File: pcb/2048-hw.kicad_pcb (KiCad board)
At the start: 2 copper layers, 60 x 100 mm, 98 parts, among them J1 UJC-HP-3-SMT-TR, J2 Battery, J3 SWD, SW1 SW_SPDT, SW2 PUSH_A, SW3 PUSH_B, U1 STM32F303K8Tx, U2 MCP73831-2-OT, U3 AP2210N-3.3TRG1, U4 PSP_1000_JSTK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

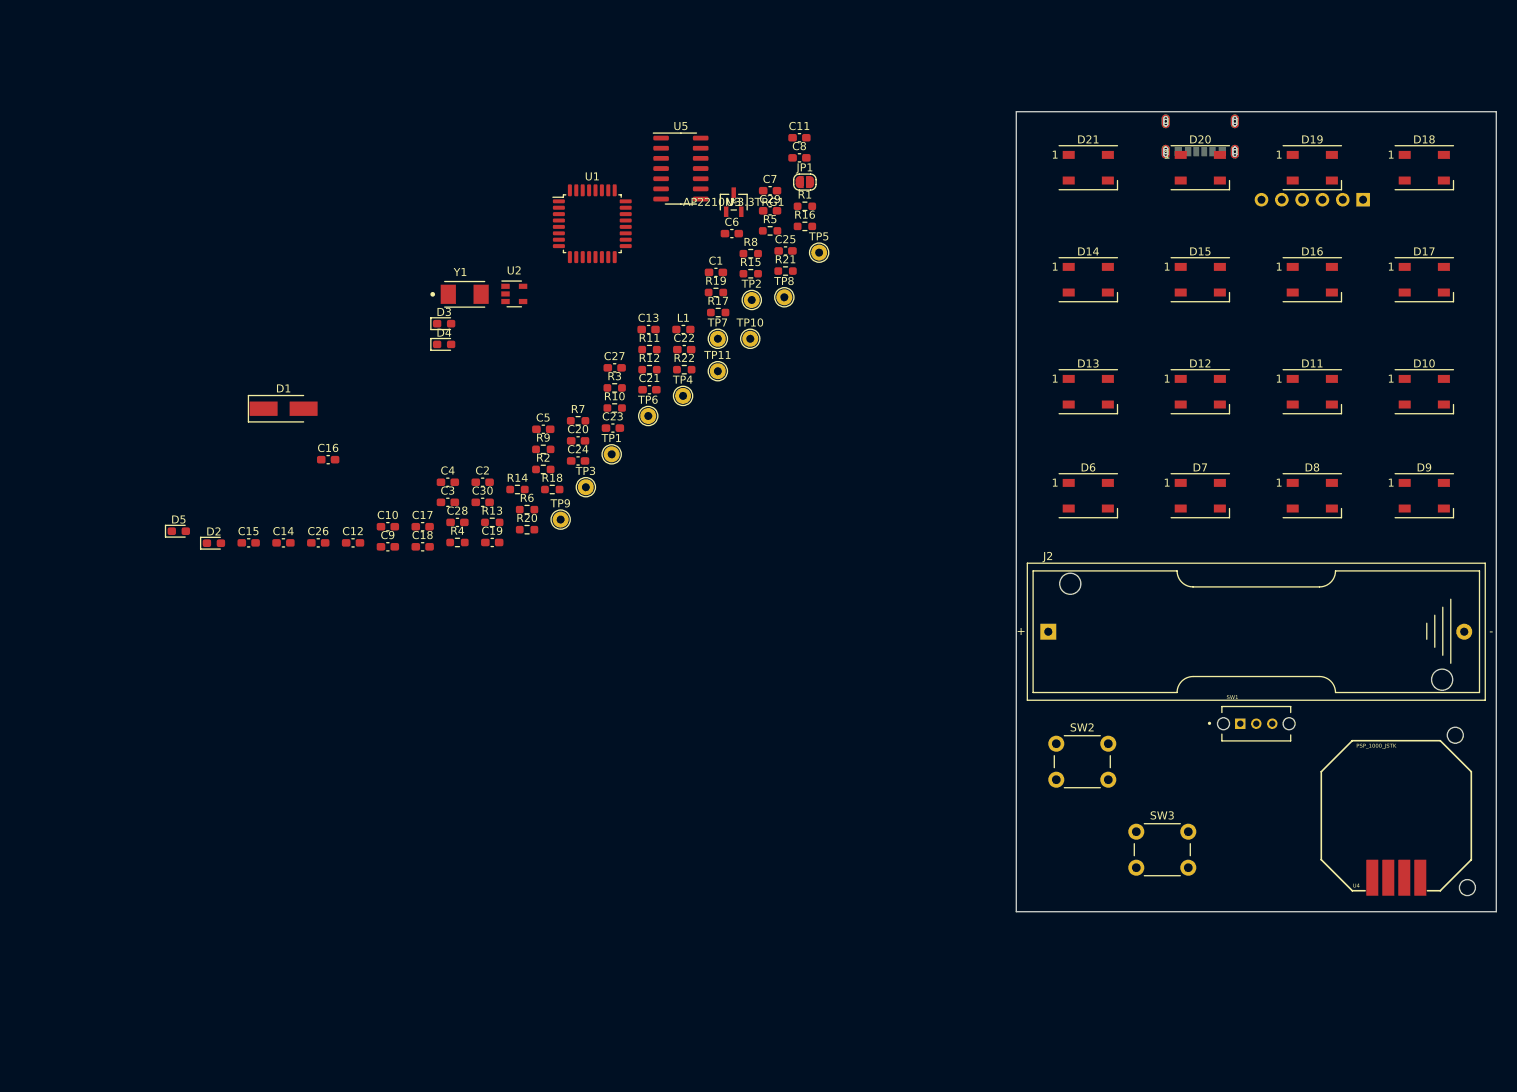
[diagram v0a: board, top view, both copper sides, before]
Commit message: Group components in layout
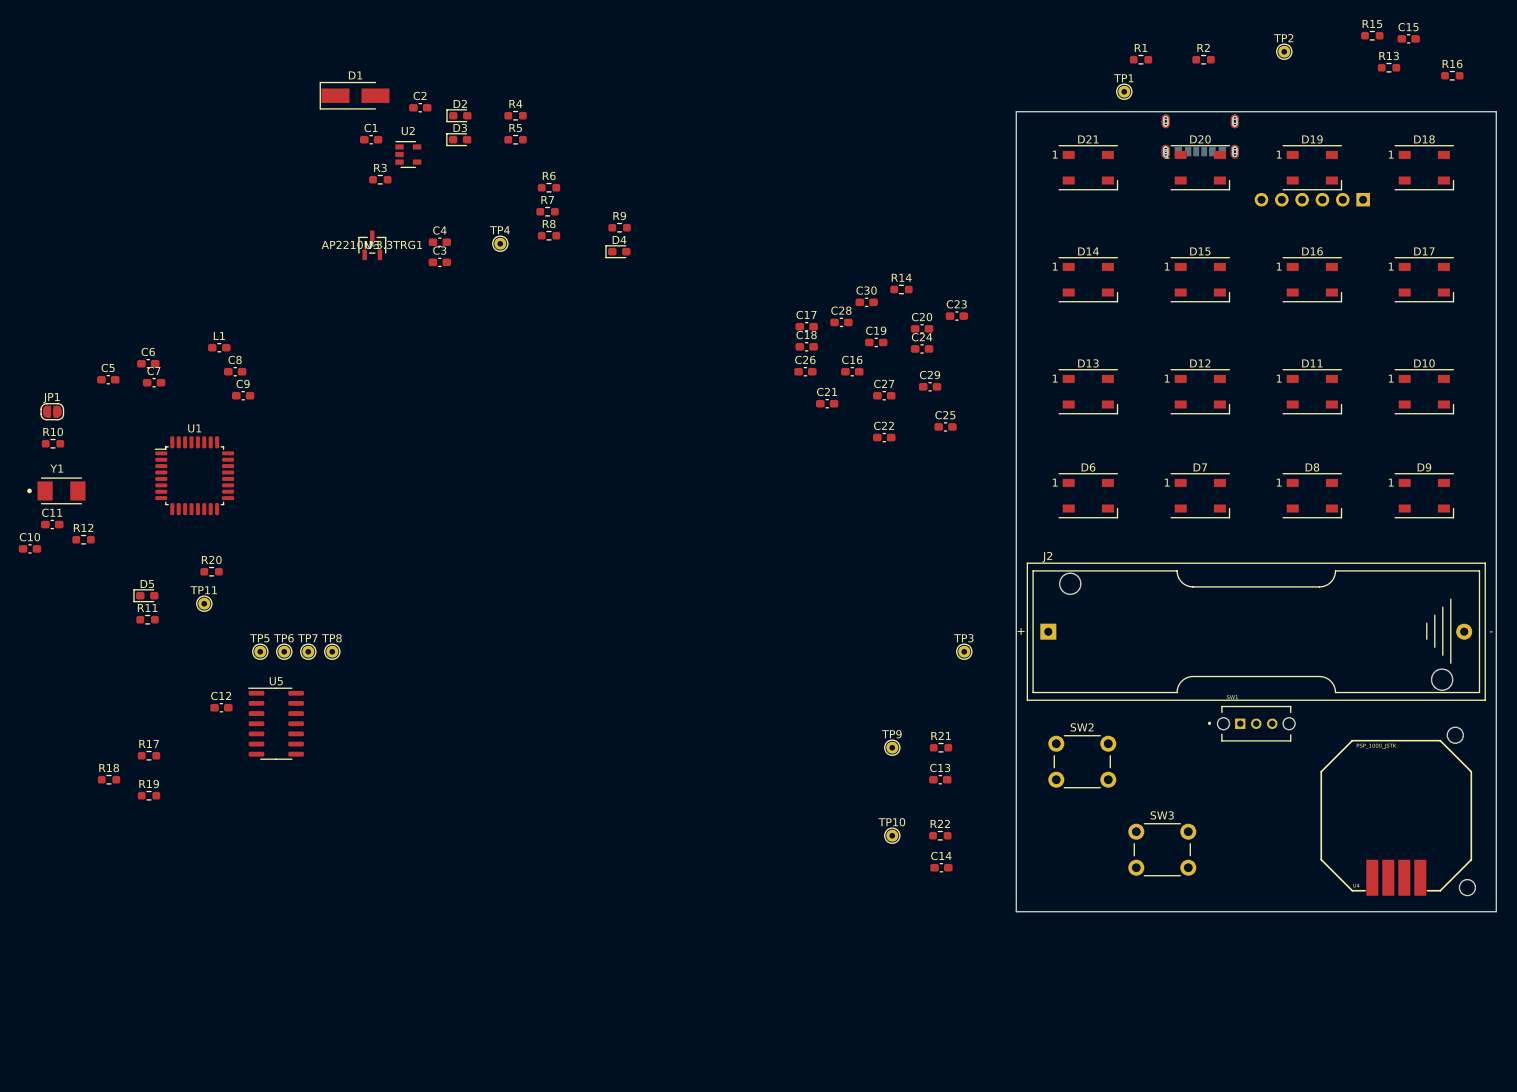
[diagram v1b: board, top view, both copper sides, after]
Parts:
- TP1, TP10, TP11, TP2, TP3, TP4, TP5, TP6, TP7, TP8, TP9: footprint TestPoint:TestPoint_THTPad_D2.0mm_Drill1.0mm -> TestPoint:TestPoint_THTPad_D1.5mm_Drill0.7mm
- moved C15 158.1 mm to (218.5, 30.4)
- moved R13 125.7 mm to (216.1, 34.0)
- moved C11 105.2 mm to (49.0, 91.1)
- moved JP1 98.4 mm to (49.0, 77.0)
- moved R2 97.1 mm to (192.9, 33.0)
- moved R19 94.8 mm to (61.1, 125.0)
- moved C14 91.7 mm to (160.1, 134.0)
- moved R17 90.2 mm to (61.1, 120.0)
- moved U5 85.9 mm to (77.0, 116.0)
- moved TP5 85.8 mm to (75.0, 107.0)
- moved R15 83.2 mm to (214.0, 30.0)
- moved R16 83.1 mm to (224.0, 35.0)
- moved C7 80.7 mm to (61.7, 73.4)
- moved TP1 78.5 mm to (183.0, 37.0)
- moved C8 75.4 mm to (71.9, 72.0)
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
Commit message: Update switches and battery
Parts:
- J2: footprint 2048-hw:BatteryHolder_Keystone_2460_1xAA -> Connector_JST:JST_PH_S2B-PH-K_1x02_P2.00mm_Horizontal; moved to B.Cu
- SW1: footprint 2048-hw:SW_OS102011MS2QN1 -> 2048-hw:E_SWITCH_EG2208A; moved to B.Cu
- moved SW1 72.6 mm to (212.0, 44.5)
- moved J3 56.1 mm to (221.0, 106.0), turned to 0 degrees
- moved C10 37.7 mm to (81.2, 108.2)
- moved C11 37.7 mm to (84.0, 105.1)
- moved C12 37.7 mm to (105.1, 128.0)
- moved C5 37.7 mm to (91.0, 87.0)
- moved C6 37.7 mm to (96.0, 85.0)
- moved C7 37.7 mm to (96.7, 87.4)
- moved C8 37.7 mm to (106.9, 86.0)
- moved C9 37.7 mm to (107.9, 89.0)
- moved D5 37.7 mm to (95.9, 114.0)
- moved JP1 37.7 mm to (84.0, 91.0)
- moved L1 37.7 mm to (104.9, 83.0)
- moved R10 37.7 mm to (84.1, 95.0)
- moved R17 37.7 mm to (96.1, 134.0)
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
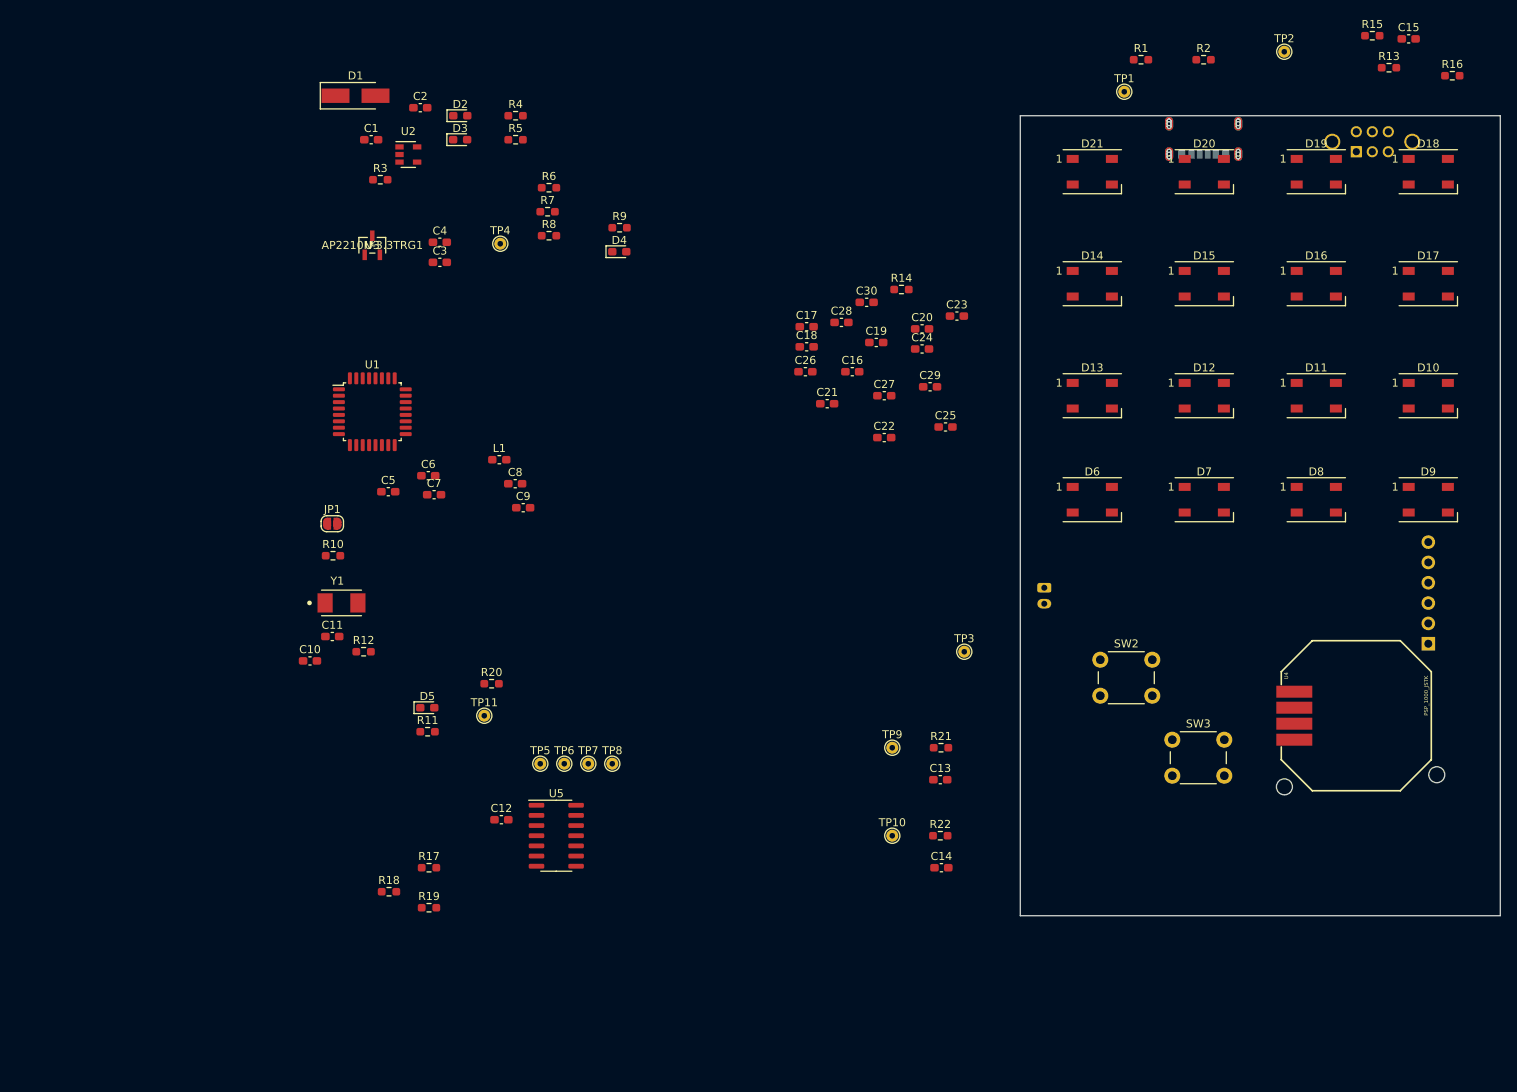
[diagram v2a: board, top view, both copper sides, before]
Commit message: Initial layout of components
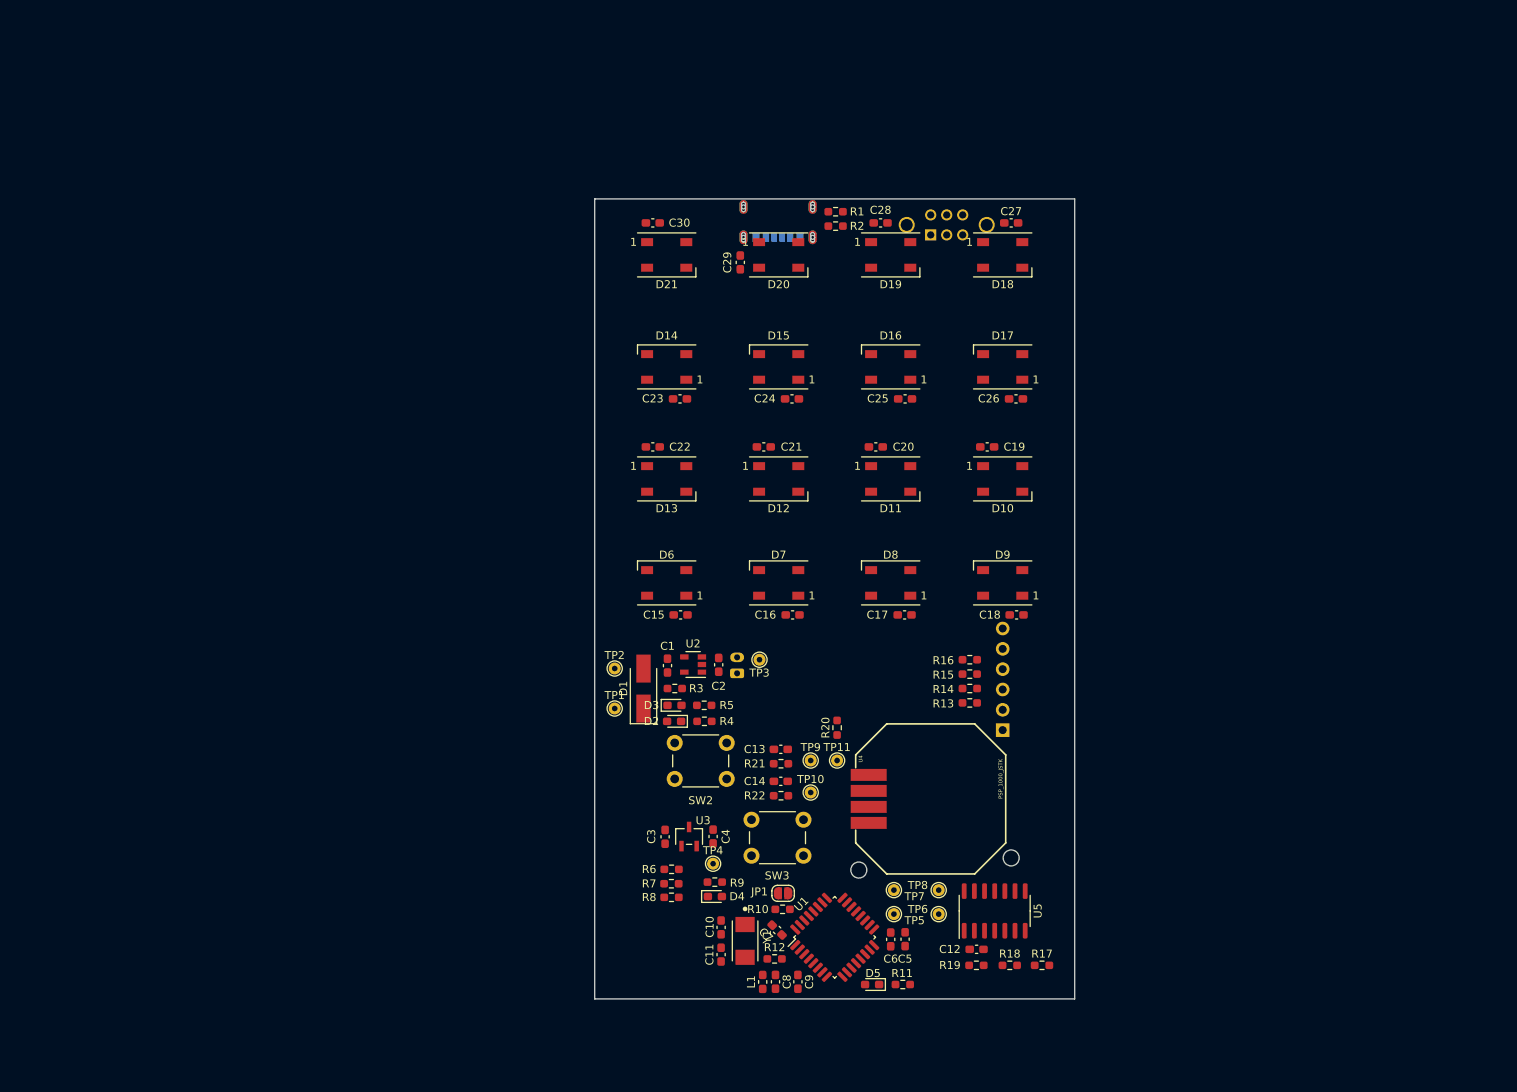
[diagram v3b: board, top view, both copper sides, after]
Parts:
- C8: value 100n -> 1u
- C9: value 100n -> 10n
- moved C15 116.0 mm to (127.5, 102.4)
- moved TP2 113.8 mm to (119.3, 109.1)
- moved TP1 100.0 mm to (119.3, 114.1)
- moved R13 95.1 mm to (163.7, 113.4), turned to 180 degrees
- moved R16 94.7 mm to (163.7, 108.0), turned to 180 degrees
- moved R15 94.3 mm to (163.7, 109.8), turned to 180 degrees
- moved U1 87.5 mm to (146.8, 142.7), turned to 45 degrees
- moved R6 86.6 mm to (126.4, 134.2), turned to 180 degrees
- moved C5 85.5 mm to (155.6, 142.9), turned to 270 degrees
- moved R7 85.4 mm to (126.4, 136.0)
- moved R8 84.1 mm to (126.4, 137.7), turned to 180 degrees
- moved U3 83.8 mm to (128.6, 130.1)
- moved R9 82.7 mm to (131.8, 135.8), turned to 180 degrees
- moved D1 82.4 mm to (122.9, 111.6), turned to 90 degrees
- moved TP4 81.9 mm to (131.6, 133.5)
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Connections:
- U1 pad 13: SPI1_MOSI -> Net-(U1-Pad13)
- U1 pad 14: PUSH_A -> Net-(U1-Pad14)
- U1 pad 15: PUSH_B -> Net-(U1-Pad15)
- U1 pad 28: Net-(U1-Pad28) -> SPI1_MOSI
- U1 pad 29: Net-(U1-Pad29) -> PUSH_A
- U1 pad 30: Net-(U1-Pad30) -> PUSH_B

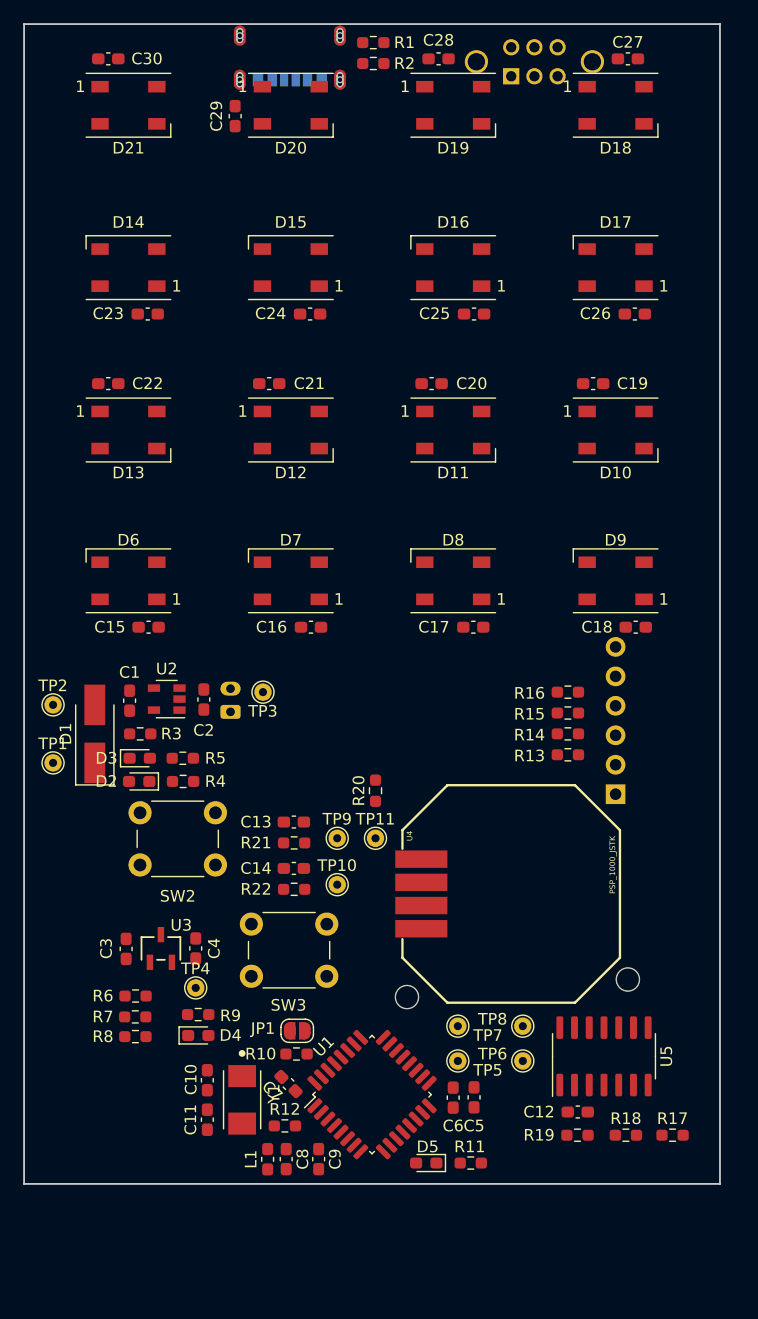
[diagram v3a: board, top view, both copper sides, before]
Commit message: Make board square
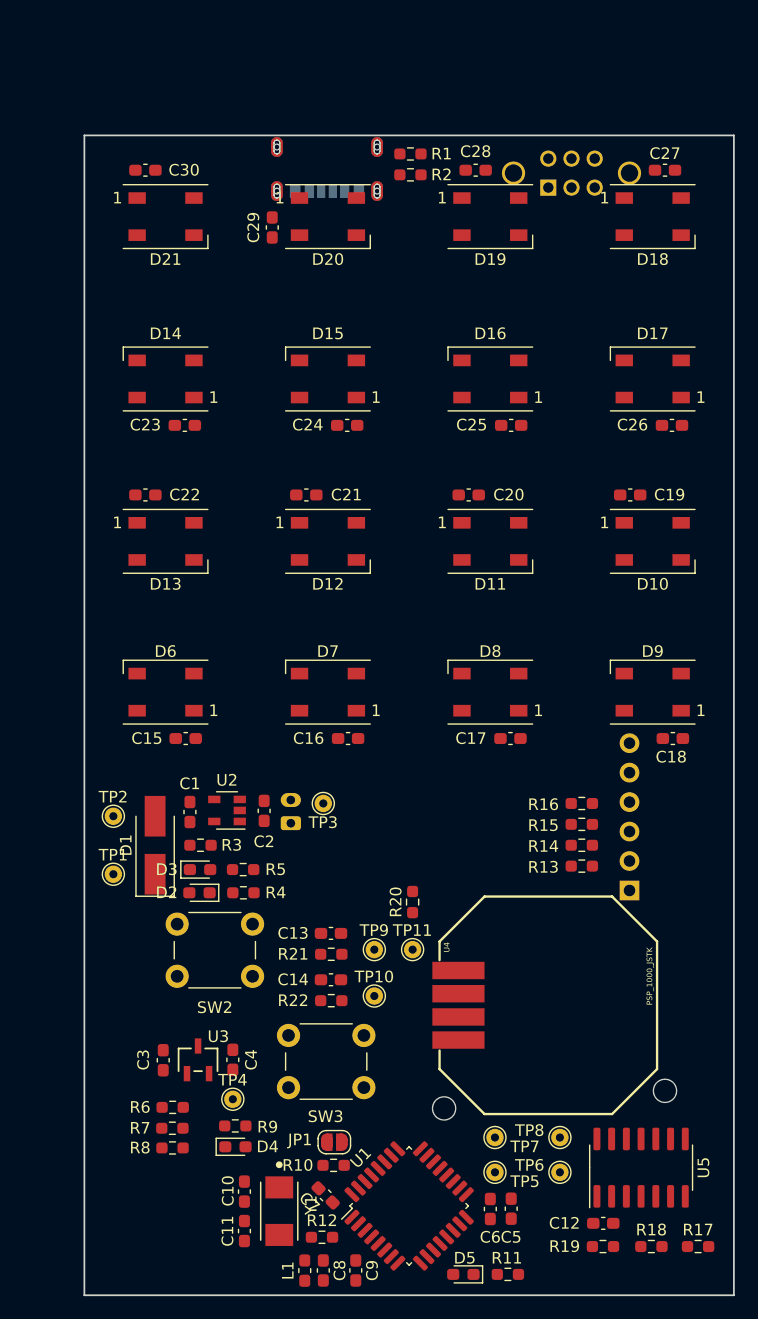
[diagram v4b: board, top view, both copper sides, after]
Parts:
- moved U2 10.9 mm to (134.3, 118.2)
- moved TP1 10.9 mm to (124.5, 123.7)
- moved TP2 10.9 mm to (124.5, 118.7)
- moved D2 10.9 mm to (131.9, 125.3)
- moved J2 10.9 mm to (139.8, 119.3)
- moved R4 10.9 mm to (135.7, 125.3)
- moved C1 10.9 mm to (131.1, 118.3)
- moved D1 10.9 mm to (128.1, 121.2)
- moved R3 10.9 mm to (132.0, 121.2)
- moved C2 10.9 mm to (137.5, 118.2)
- moved D3 10.9 mm to (132.0, 123.3)
- moved R5 10.9 mm to (135.7, 123.3)
- moved TP3 10.9 mm to (142.6, 117.6)
- moved C3 10.1 mm to (128.8, 139.7)
- moved C9 10.1 mm to (145.4, 157.9)
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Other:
- board size 60 x 100 mm -> 56 x 100 mm
